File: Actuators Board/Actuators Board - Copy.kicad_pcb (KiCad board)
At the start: 2 copper layers, 96 parts, among them IC1 BD62120AEFJ-E2, J10 Conn_01x02_Male, J3 USB_C_Receptacle_USB2.0, J4 Conn_01x03_Male, J5 Conn_01x06_Male, J9 Conn_01x02_Male, Q1 MMDT2222A, Q2 SI2366DS, U1 ESP32-PICO-D4, U2 TPS54233D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

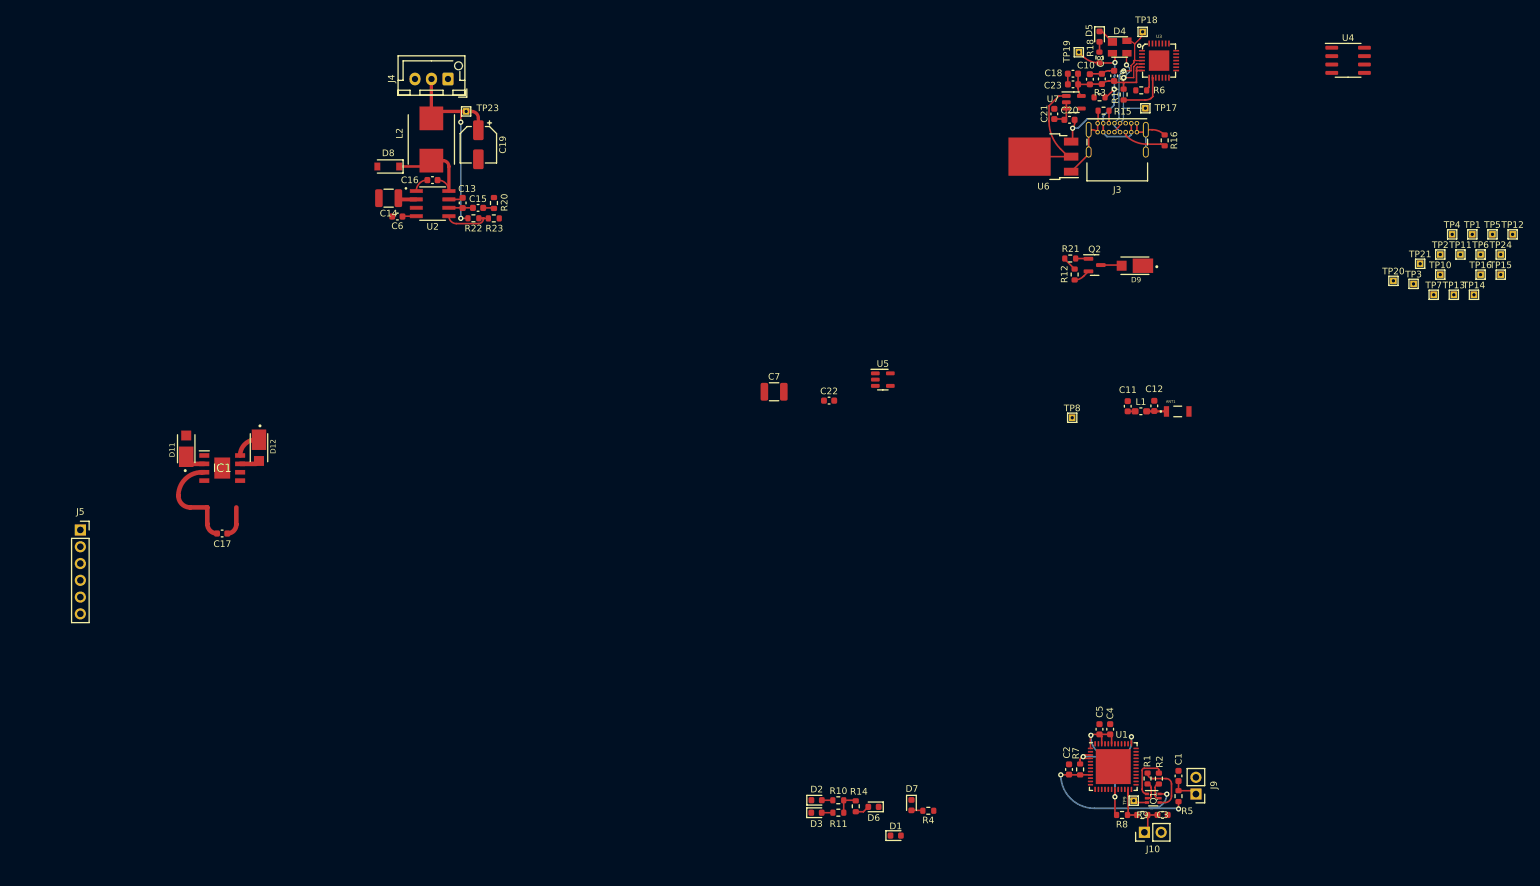
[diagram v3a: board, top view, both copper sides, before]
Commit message: SOL and U5 connections added
copies of the files also made. Connections are about the bottom and U5 is at the right side.
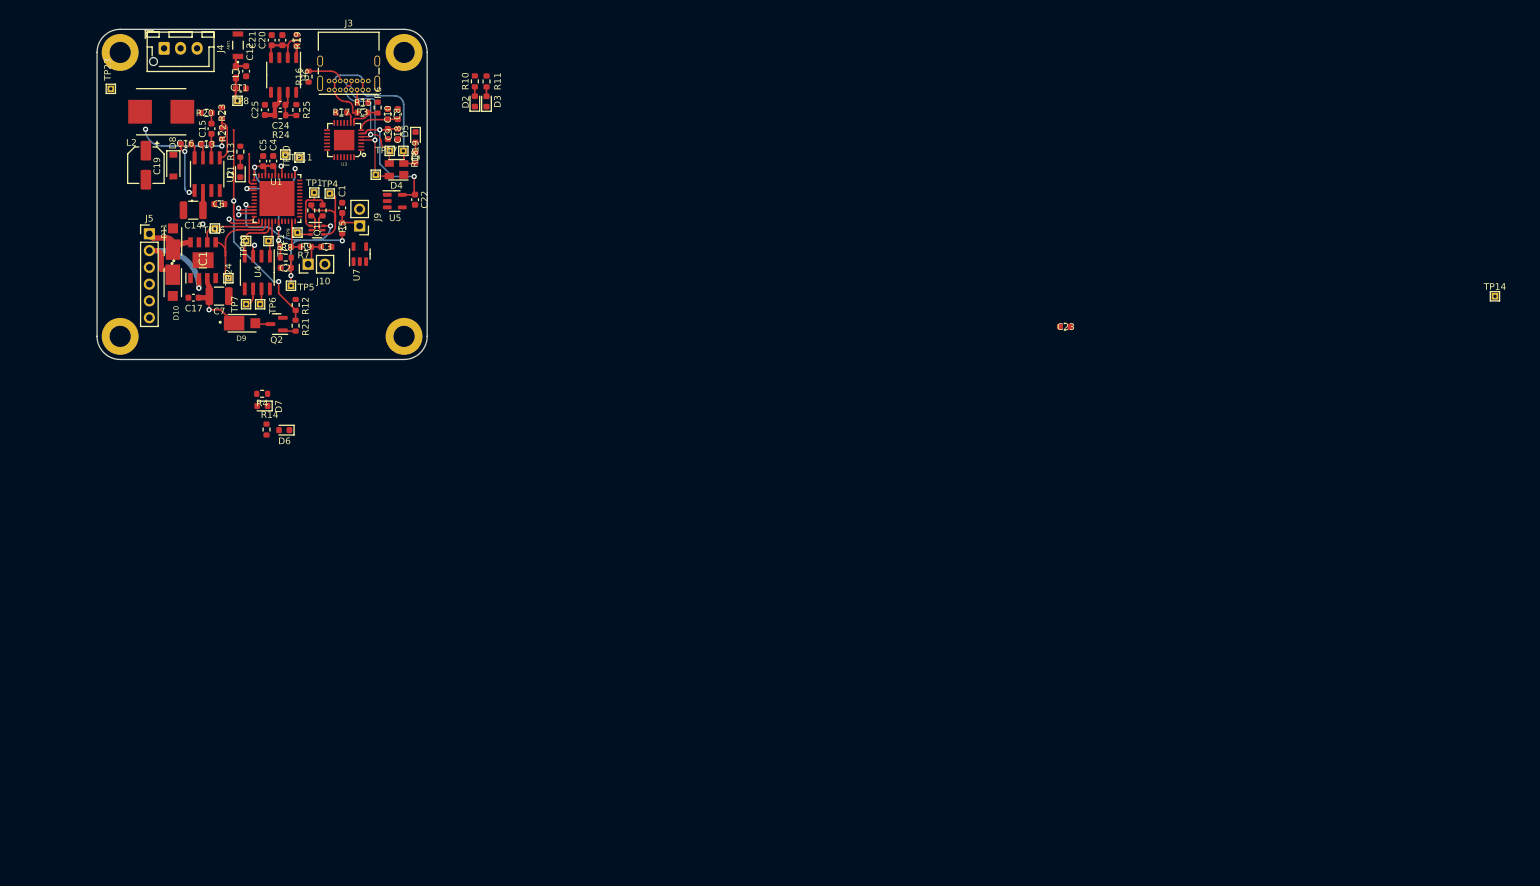
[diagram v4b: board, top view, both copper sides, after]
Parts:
- removed TP12, TP13, TP15, TP2, TP3: TestPoint, TestPoint:TestPoint_THTPad_1.0x1.0mm_Drill0.5mm
- added C24: 0.1uF, Capacitor_SMD:C_0603_1608Metric, F.Cu at (82.8, 41.4)
- added C25: 10uF, Capacitor_SMD:C_0603_1608Metric, F.Cu at (80.4, 42.2)
- added H1: MountingHole_Pad, MountingHole:MountingHole_3.2mm_M3_DIN965_Pad, F.Cu at (58.5, 76.5)
- added H2: MountingHole_Pad, MountingHole:MountingHole_3.2mm_M3_DIN965_Pad, F.Cu at (101.5, 33.5)
- added H3: MountingHole_Pad, MountingHole:MountingHole_3.2mm_M3_DIN965_Pad, F.Cu at (101.5, 76.5)
- added H4: MountingHole_Pad, MountingHole:MountingHole_3.2mm_M3_DIN965_Pad, F.Cu at (58.5, 33.5)
- added R13: 470, Resistor_SMD:R_0603_1608Metric, F.Cu at (76.7, 48.5)
- added R19: 100k, Resistor_SMD:R_0603_1608Metric, F.Cu at (85.2, 31.6)
- added R24: 147k, Resistor_SMD:R_0603_1608Metric, F.Cu at (82.8, 43.0)
- added R25: 47k, Resistor_SMD:R_0603_1608Metric, F.Cu at (85.2, 42.2)
- C21: value 22uF -> 1uF
- J5: footprint Connector_PinSocket_2.54mm:PinSocket_1x06_P2.54mm_Vertical -> Connector_PinHeader_2.54mm:PinHeader_1x06_P2.54mm_Vertical
- U6: value AZ1084-3.3 -> RT9025-25GSP; footprint Package_TO_SOT_SMD:TO-252-3_TabPin2 -> Package_SO:SOP-8_3.9x4.9mm_P1.27mm
- moved TP24 192.7 mm to (74.9, 67.7)
- moved TP16 191.8 mm to (72.9, 60.2)
- moved TP6 185.0 mm to (79.7, 71.6)
- moved TP5 182.1 mm to (84.4, 68.8)
- moved TP7 179.9 mm to (77.6, 71.6)
- moved TP11 176.5 mm to (85.7, 49.4)
- moved TP10 175.9 mm to (83.5, 49.0)
- moved TP1 175.5 mm to (87.9, 54.7)
- moved TP21 174.5 mm to (81.0, 62.1)
- moved TP20 173.9 mm to (77.6, 62.0)
- moved TP4 170.1 mm to (90.2, 54.9)
- moved U4 168.3 mm to (79.3, 66.8), turned to -90 degrees
- moved C4 153.2 mm to (81.7, 50.0)
- moved J10 153.1 mm to (87.0, 65.6)
- moved C1 153.1 mm to (92.1, 57.0)
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- renumbered D11 to D10, D12 to D11
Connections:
- C21 pad 2: (no net) -> VBUS
- D1 pad 2: /SolEN -> Net-(D1-Pad2)
- R3 pad 2: (no net) -> Net-(R3-Pad2)
- U1 pad 10: unconnected-(U1-Pad10) -> /Hall1
- U1 pad 11: unconnected-(U1-Pad11) -> /Hall2
- U1 pad 12: /CAN_TX -> /SolEN
- U1 pad 13: /CAN_RX -> /ServoPWM
- U1 pad 14: unconnected-(U1-Pad14) -> /HBridgeDIR2
- U1 pad 16: /HBridgeDIR2 -> /CAN_RX
- U1 pad 17: /ServoPWM -> /CAN_TX
- U1 pad 21: /SolEN -> unconnected-(U1-Pad21)
- U1 pad 24: /Hall2 -> unconnected-(U1-Pad24)
- U1 pad 34: /Hall1 -> unconnected-(U1-Pad34)
- U5 pad 1: (no net) -> Net-(J1-Pad4)
- U5 pad 4: (no net) -> unconnected-(U5-Pad4)
- U6 pad 1: GND -> Net-(R19-Pad1)
- U6 pad 2: Net-(C21-Pad2) -> VBUS
- U7 pad 1: Net-(C21-Pad2) -> Net-(C24-Pad2)
- U7 pad 4: (no net) -> unconnected-(U7-Pad4)
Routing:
- net GND: track 46.6 -> 2.21 mm
- net /SolEN: track 2.20 -> 39.5 mm, vias 0 -> 2
- net +6V: track 33.4 -> 14.2 mm
- net Net-(C21-Pad2): track 18.6 -> 0.00 mm
- net /HBridgeDIR1: track 0.00 -> 16.6 mm
- net /Motor-: track 3.14 -> 19.5 mm, vias 0 -> 1
- net Net-(C16-Pad2): track 14.8 -> 2.34 mm
- net /HBridgeDIR2: track 0.00 -> 10.4 mm
- net +3V3: track 59.0 -> 68.4 mm, vias 4 -> 8
- net /CAN_RX: track 0.00 -> 8.24 mm
- net /LNA_IN: track 1.44 -> 8.80 mm
- net Net-(C16-Pad1): track 2.55 -> 8.93 mm, vias 0 -> 2
- net /CAN_TX: track 0.00 -> 5.69 mm
- net Net-(R17-Pad2): track 7.44 -> 1.89 mm
- net Net-(C24-Pad2): track 0.00 -> 5.39 mm
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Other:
- board outline added: 50 x 50 mm

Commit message: curves
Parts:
- moved TP14 141.6 mm to (125.6, 82.4)
- moved C23 103.3 mm to (99.0, 63.2)
- moved U7 0.40 mm to (95.2, 64.2), turned to 0 degrees
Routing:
- net +3V3: track 68.4 -> 70.1 mm

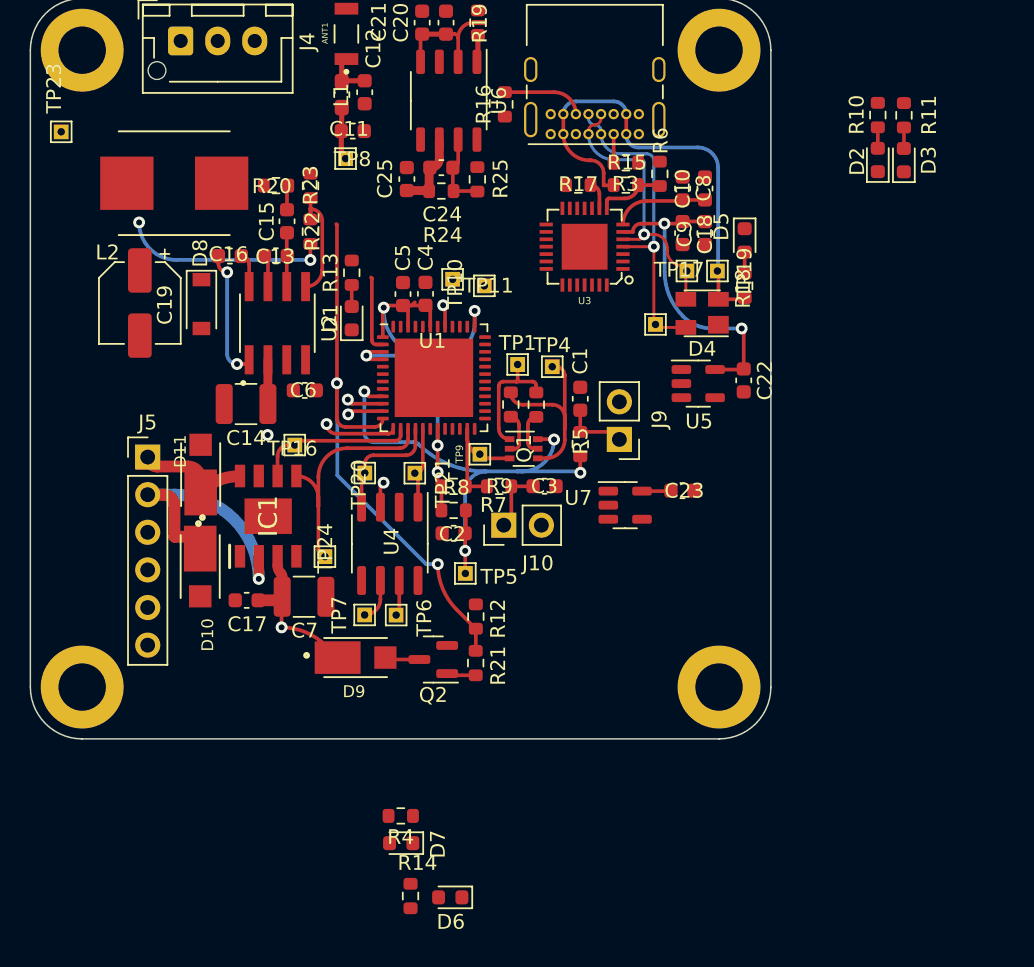
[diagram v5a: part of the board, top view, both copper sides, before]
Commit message: LEDs connected and sol led moved
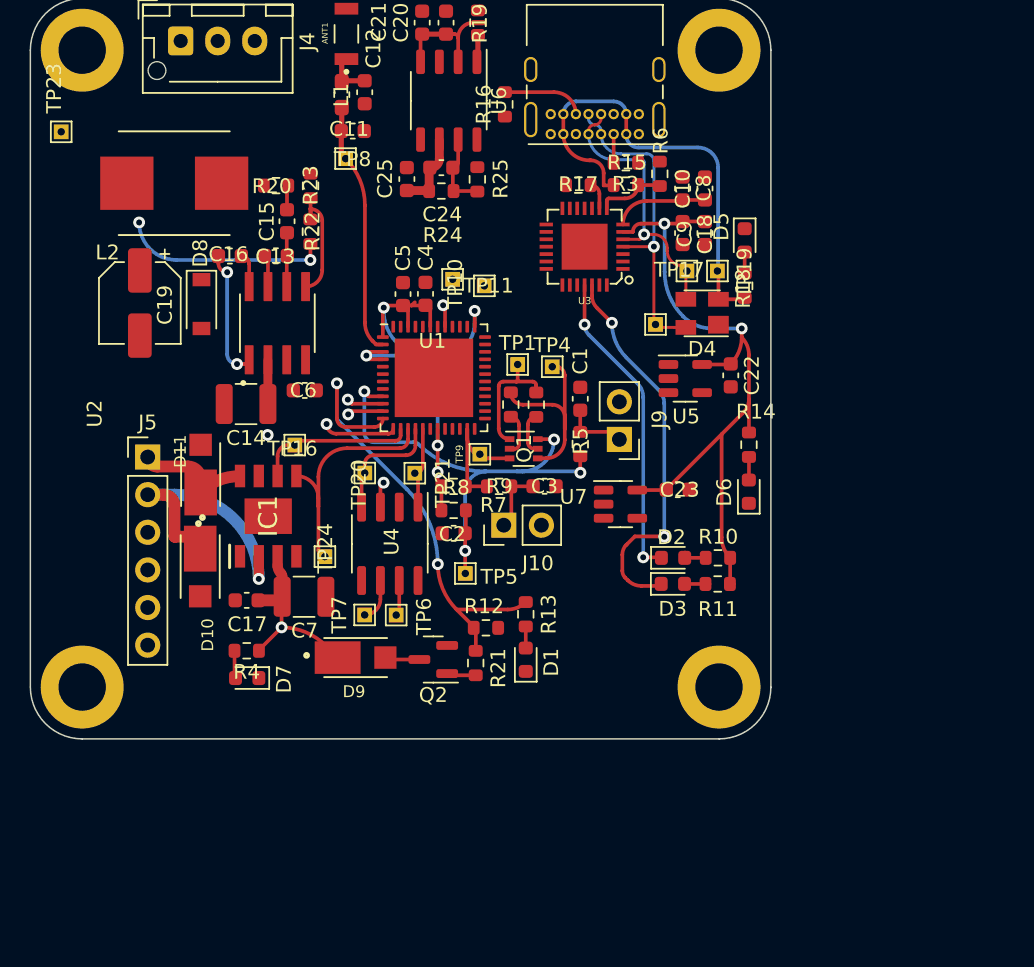
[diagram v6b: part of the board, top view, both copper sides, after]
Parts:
- moved R14 38.1 mm to (103.5, 60.1)
- moved R11 34.1 mm to (101.4, 69.5), turned to 180 degrees
- moved D6 34.0 mm to (103.5, 63.3), turned to 90 degrees
- moved D3 32.6 mm to (98.4, 69.5), turned to 0 degrees
- moved R10 31.8 mm to (101.4, 67.8), turned to 180 degrees
- moved D2 30.2 mm to (98.4, 67.8), turned to 0 degrees
- moved D1 25.9 mm to (88.5, 74.7)
- moved R13 25.9 mm to (88.5, 71.6)
- moved D7 15.2 mm to (69.6, 75.9)
- moved R4 15.2 mm to (69.6, 74.0)
- moved R12 1.02 mm to (85.8, 72.5), turned to 0 degrees
- moved C22 0.94 mm to (102.3, 55.5)
- moved U5 0.94 mm to (99.2, 55.7)
- moved C23 0.33 mm to (98.7, 63.2)
- moved U7 0.33 mm to (94.8, 64.2)
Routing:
- net /TXD: track 0.00 -> 26.5 mm, vias 0 -> 2
- net +3V3: track 70.1 -> 94.9 mm
- net /RXD: track 1.56 -> 22.7 mm, vias 1 -> 3
- net /LNA_IN: track 8.80 -> 17.2 mm
- net /SolEN: track 39.3 -> 32.6 mm
- net +24V: track 14.5 -> 16.7 mm
- net Net-(D7-Pad2): track 0.00 -> 1.86 mm
- net Net-(D6-Pad2): track 0.00 -> 1.56 mm

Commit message: most of board copy sorted
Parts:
- removed TP8: TestPoint, TestPoint:TestPoint_THTPad_1.0x1.0mm_Drill0.5mm
- added ?: , , F.Cu at (87.1, 74.3)
- added C26: 100pF, Capacitor_SMD:C_0603_1608Metric, F.Cu at (82.8, 43.6)
- added C27: 10uF, Capacitor_SMD:C_0603_1608Metric, F.Cu at (74.7, 48.0)
- added C28: 1uF, Capacitor_SMD:C_0603_1608Metric, F.Cu at (76.2, 48.0)
- added C29: 0.1uF, Capacitor_SMD:C_0603_1608Metric, F.Cu at (77.7, 48.0)
- added C30: 0.1uF, Capacitor_SMD:C_0603_1608Metric, F.Cu at (84.5, 54.9)
- added C31: 0.1uF, Capacitor_SMD:C_0603_1608Metric, F.Cu at (87.0, 44.4)
- added J1: Conn_01x05_Male, Connector_PinHeader_2.54mm:PinHeader_1x05_P2.54mm_Vertical, F.Cu at (78.6, 77.6)
- added J2: Solenoid(Sol), Connector_PinHeader_2.54mm:PinHeader_1x02_P2.54mm_Vertical, F.Cu at (83.8, 77.7)
- added JP1: SolderJumper_2_Open, Jumper:SolderJumper-2_P1.3mm_Open_RoundedPad1.0x1.5mm, F.Cu at (44.0, 50.1)
- added TP12: TestPoint, TestPoint:TestPoint_THTPad_1.0x1.0mm_Drill0.5mm, F.Cu at (72.0, 37.8)
- added TP2: TestPoint, TestPoint:TestPoint_THTPad_1.0x1.0mm_Drill0.5mm, F.Cu at (61.1, 58.6)
- added TP3: TestPoint, TestPoint:TestPoint_THTPad_1.0x1.0mm_Drill0.5mm, F.Cu at (61.1, 60.7)
- C4: value 10uF -> 0.1uF
- C5: value 0.1uF -> 1uF
- TP20, TP21, TP6, TP7: footprint TestPoint:TestPoint_THTPad_1.0x1.0mm_Drill0.5mm -> TestPoint:TestPoint_Pad_D1.0mm
- U2: footprint iclr:SOIC127P599X175-8N -> Package_SO:SOIC-8-1EP_3.9x4.9mm_P1.27mm_EP2.29x3mm_ThermalVias
- moved C21 42.7 mm to (102.0, 69.1), turned to 90 degrees
- moved C20 41.3 mm to (100.4, 69.1), turned to 90 degrees
- moved TP14 39.9 mm to (89.4, 65.5)
- moved R19 39.6 mm to (98.3, 69.1), turned to -90 degrees
- moved R10 35.2 mm to (84.0, 37.1), turned to 0 degrees
- moved D6 32.6 mm to (71.2, 67.8)
- moved D2 32.2 mm to (86.3, 37.9), turned to 90 degrees
- moved U6 31.8 mm to (100.2, 63.8), turned to 90 degrees
- moved C22 31.5 mm to (73.7, 68.5), turned to 180 degrees
- moved R14 30.7 mm to (73.6, 67.0), turned to 0 degrees
- moved U5 28.5 mm to (75.4, 71.3), turned to 90 degrees
- moved C25 27.7 mm to (102.8, 58.6), turned to 90 degrees
- moved C24 25.2 mm to (100.5, 59.3), turned to 0 degrees
- moved R24 23.1 mm to (100.5, 57.8), turned to 180 degrees
- moved R25 20.9 mm to (98.3, 58.6), turned to -90 degrees
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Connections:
- C4 pad 1: GND -> +3V3
- C4 pad 2: +3V3 -> GND
- IC1 pad 2: /Motor- -> /Motor+
- IC1 pad 8: /Motor+ -> /Motor-
- U1 pad 10: /Hall1 -> /ServoPWM
- U1 pad 12: /SolEN -> /Hall1
- U1 pad 13: /ServoPWM -> unconnected-(U1-Pad13)
- U1 pad 34: unconnected-(U1-Pad34) -> /SolEN
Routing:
- net +24V: track 16.7 -> 65.0 mm, vias 2 -> 1
- net VBUS: track 40.1 -> 72.3 mm
- net /Hall1: track 2.51 -> 30.3 mm, vias 1 -> 0
- net /Hall2: track 2.46 -> 28.2 mm, vias 1 -> 0
- net /CAN_LOW: track 2.89 -> 26.3 mm, vias 0 -> 1
- net /ServoPWM: track 5.02 -> 26.1 mm, vias 1 -> 0
- net +6V: track 14.2 -> 32.5 mm, vias 2 -> 0
- net /CAN_HIGH: track 2.44 -> 16.2 mm
- net Net-(C16-Pad2): track 2.34 -> 15.0 mm
- net /EN: track 36.0 -> 48.6 mm
- net /HBridgeDIR2: track 10.4 -> 22.9 mm
- net +3V3: track 94.9 -> 105.6 mm, vias 8 -> 4
- net /DTR: track 13.3 -> 22.8 mm, vias 0 -> 2
- net /Motor-: track 19.5 -> 10.6 mm, vias 1 -> 0
- net /RTS: track 8.47 -> 17.0 mm, vias 0 -> 2
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- added copper zone on B.Cu, net GND
- added copper zone on F.Cu, net GND
